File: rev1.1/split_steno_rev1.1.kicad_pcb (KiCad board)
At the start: 2 copper layers, 99.4 x 84.8 mm, 77 parts, among them J1 i2c, J2 serial, J3 rgb, J4 icsp, J5 raw, J6 extra, Q1 BC547, SW1 reset, U1 ProMicro

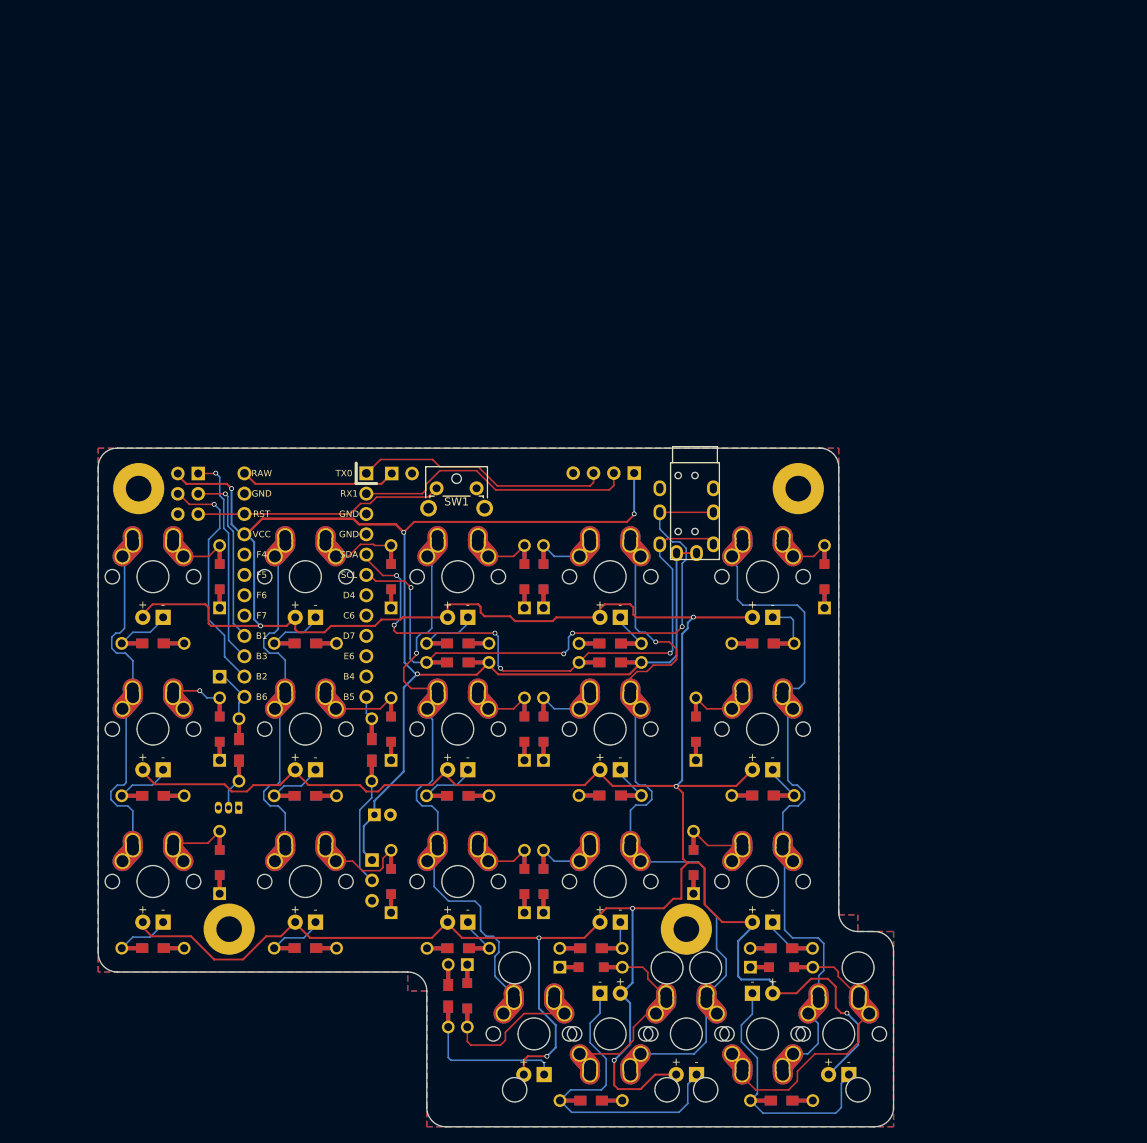
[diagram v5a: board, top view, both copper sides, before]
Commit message: removed led from rev1.1, moved to rev1.2
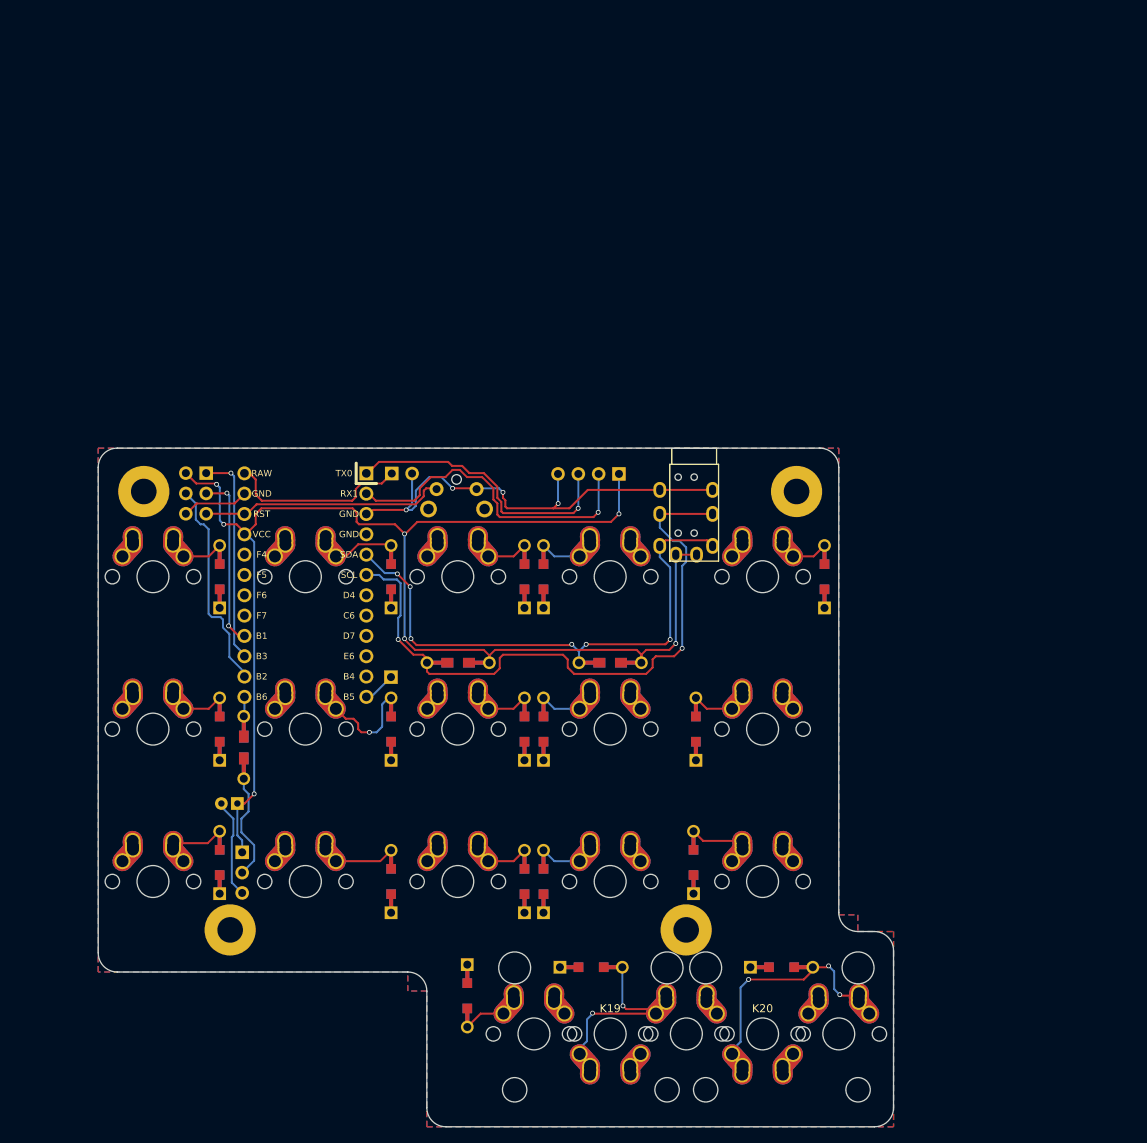
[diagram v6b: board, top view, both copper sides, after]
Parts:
- removed the G*** at (96.1, 158.9) (x2)
- removed MX1, MX10, MX11, MX12, MX13, MX14, MX15, MX16, MX18, MX2, MX20, MX3, MX4, MX5, MX6, MX7, MX8, MX9: MX-1U, Keebio-Parts:Hybrid_PCB_100H_Dual_hole-LED
- removed MX17, MX19: MX-1U, Keebio-Parts:Hybrid_PCB_200H-dual-LED
- removed Q1: BC547, TO_SOT_Packages_THT:TO-92_Inline_Narrow_Oval
- removed R10, R11, R12, R13, R14, R15, R16, R17, R18, R4, R5, R6, R7, R8, R9: 51, Keebio-Parts:Resistor-Hybrid
- removed R19: 470, Keebio-Parts:Resistor-Hybrid
- removed R20: 1k, Keebio-Parts:Resistor-Hybrid
- removed R21, R22: 4.7k, Keebio-Parts:Resistor-Hybrid
- removed the REF** at (55.4, 84.2)
- removed the REF** at (137.8, 84.2)
- removed the REF** at (123.8, 139.3)
- removed the REF** at (66.7, 139.3)
- added G***: LOGO, airi_logo:airi_icon-7.6, B.Cu at (96.2, 159.2)
- added G***: LOGO, airi_logo:airi_icon-7.6, F.Cu at (96.2, 159.2)
- added K1: KEYSW, Keebio-Parts:Hybrid_PCB_100H_Dual_hole, F.Cu at (57.1, 95.2)
- added K10: KEYSW, Keebio-Parts:Hybrid_PCB_100H_Dual_hole-flip, F.Cu at (133.3, 114.3)
- added K11: KEYSW, Keebio-Parts:Hybrid_PCB_100H_Dual_hole, F.Cu at (57.1, 133.3)
- added K12: KEYSW, Keebio-Parts:Hybrid_PCB_100H_Dual_hole, F.Cu at (76.2, 133.3)
- added K13: KEYSW, Keebio-Parts:Hybrid_PCB_100H_Dual_hole, F.Cu at (95.2, 133.3)
- added K14: KEYSW, Keebio-Parts:Hybrid_PCB_100H_Dual_hole-flip, F.Cu at (114.3, 133.3)
- added K15: KEYSW, Keebio-Parts:Hybrid_PCB_100H_Dual_hole-flip, F.Cu at (133.3, 133.3)
- added K16: KEYSW, Keebio-Parts:Hybrid_PCB_100H_Dual_hole-flip, F.Cu at (104.8, 152.4)
- added K17: KEYSW, Keebio-Parts:Hybrid_PCB_100H_Dual_hole-flip, F.Cu at (123.8, 152.4)
- added K18: KEYSW, Keebio-Parts:Hybrid_PCB_100H_Dual_hole, F.Cu at (142.9, 152.4)
- added K19: KEYSW, Keebio-Parts:Hybrid_PCB_200H-dual-nosilk, F.Cu at (114.3, 152.4)
- added K2: KEYSW, Keebio-Parts:Hybrid_PCB_100H_Dual_hole, F.Cu at (76.2, 95.2)
- added K20: KEYSW, Keebio-Parts:Hybrid_PCB_200H-dual-nosilk, F.Cu at (133.3, 152.4)
- added K3: KEYSW, Keebio-Parts:Hybrid_PCB_100H_Dual_hole, F.Cu at (95.2, 95.2)
- added K4: KEYSW, Keebio-Parts:Hybrid_PCB_100H_Dual_hole-flip, F.Cu at (114.3, 95.2)
- added K5: KEYSW, Keebio-Parts:Hybrid_PCB_100H_Dual_hole, F.Cu at (133.3, 95.2)
- added K6: KEYSW, Keebio-Parts:Hybrid_PCB_100H_Dual_hole, F.Cu at (57.1, 114.3)
- added K7: KEYSW, Keebio-Parts:Hybrid_PCB_100H_Dual_hole, F.Cu at (76.2, 114.3)
- added K8: KEYSW, Keebio-Parts:Hybrid_PCB_100H_Dual_hole, F.Cu at (95.2, 114.3)
- added K9: KEYSW, Keebio-Parts:Hybrid_PCB_100H_Dual_hole-flip, F.Cu at (114.3, 114.3)
- added REF**: , Mounting_Holes:MountingHole_3.2mm_M3_Pad, F.Cu at (56.0, 84.6)
- added REF**: , Mounting_Holes:MountingHole_3.2mm_M3_Pad, F.Cu at (137.6, 84.6)
- added REF**: , Mounting_Holes:MountingHole_3.2mm_M3_Pad, F.Cu at (66.8, 139.4)
- added REF**: , Mounting_Holes:MountingHole_3.2mm_M3_Pad, F.Cu at (123.8, 139.4)
- R1, R2: value 51 -> 4.7k
- R3: value 51 -> 470
- REF**: value i2c -> TRRS-PJ-320A
- SW1: moved to B.Cu
- moved R1 57.2 mm to (114.3, 106.0)
- moved R3 29.7 mm to (68.5, 116.6), turned to 270 degrees
- moved J6 21.4 mm to (86.9, 107.8)
- moved R2 19.3 mm to (95.3, 106.0)
- moved C1 17.2 mm to (67.7, 123.6), turned to 180 degrees
- moved J3 16.3 mm to (68.3, 129.7)
- moved SW1 5.00 mm to (97.6, 84.3), turned to 180 degrees
- moved J2 1.90 mm to (115.4, 82.4)
- moved J4 1.00 mm to (63.8, 82.3)
- moved REF** 0.22 mm to (124.8, 81.2)
- moved J1 0.20 mm to (122.8, 81.2)
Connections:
- J6 pad 1: /d4 -> /d3
- R1 pad 1: Net-(MX1-Pad4) -> /d1
- R1 pad 2: Net-(Q1-Pad1) -> VCC
- R2 pad 1: Net-(MX2-Pad4) -> /d2
- R2 pad 2: Net-(Q1-Pad1) -> VCC
- R3 pad 1: Net-(MX3-Pad4) -> Net-(J3-Pad2)
- R3 pad 2: Net-(Q1-Pad1) -> /d4
- SW1 pad 1: /rst -> GND
- SW1 pad 2: GND -> /rst
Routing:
- net VCC: track 595.1 -> 181.4 mm, vias 12 -> 7
- net /c4: track 87.6 -> 0.00 mm, vias 1 -> 0
- net GND: track 0.00 -> 79.9 mm, vias 0 -> 4
- net /c5: track 78.5 -> 0.00 mm
- net /c3: track 68.7 -> 0.00 mm, vias 1 -> 0
- net /c1: track 43.0 -> 0.00 mm
- net /c2: track 41.4 -> 0.00 mm
- net Net-(MX17-Pad4): track 40.5 -> 0.00 mm
- net Net-(MX19-Pad4): track 32.0 -> 0.00 mm
- net Net-(MX16-Pad4): track 17.5 -> 0.00 mm
- net Net-(D16-Pad2): track 18.8 -> 6.42 mm
- net /d1: track 78.2 -> 68.3 mm, vias 5 -> 6
- net Net-(MX3-Pad4): track 6.96 -> 0.00 mm
- net Net-(MX6-Pad4): track 6.87 -> 0.00 mm
- net Net-(MX8-Pad4): track 6.81 -> 0.00 mm
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
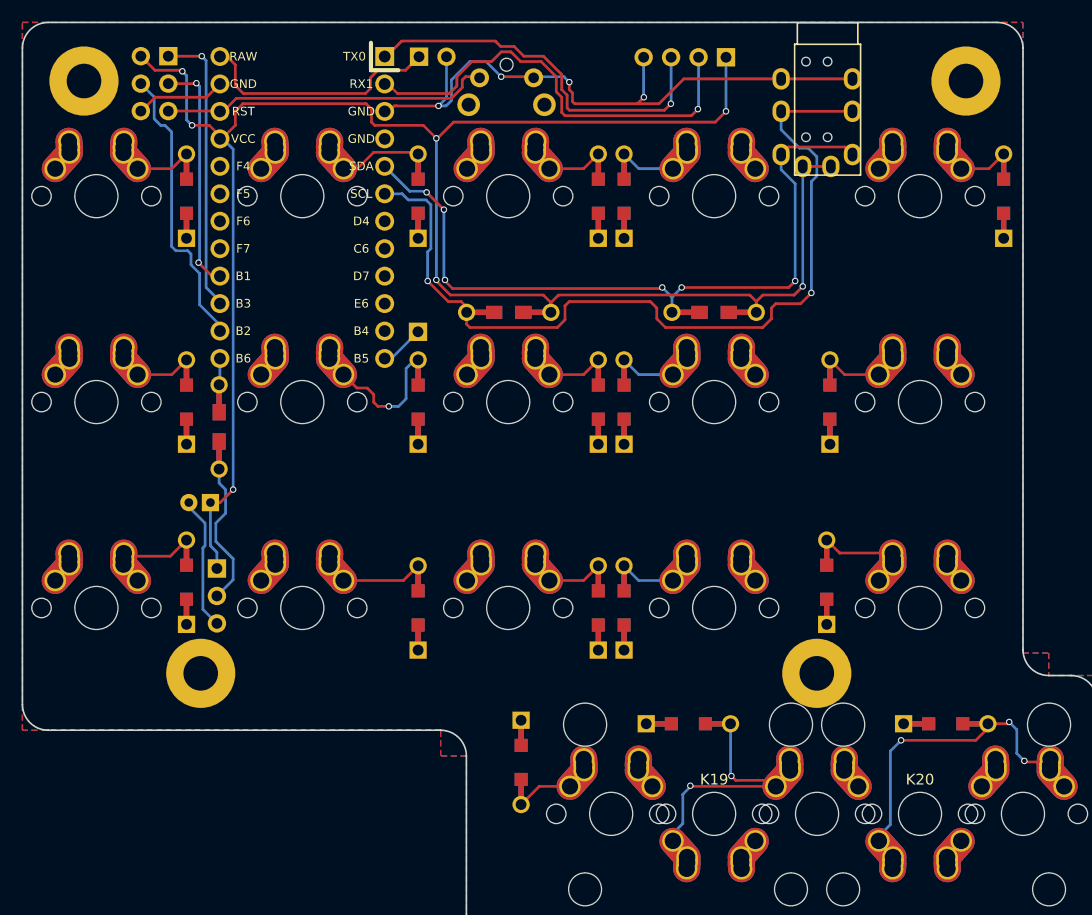
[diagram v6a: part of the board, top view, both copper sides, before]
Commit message: finished routing, added silkscreen
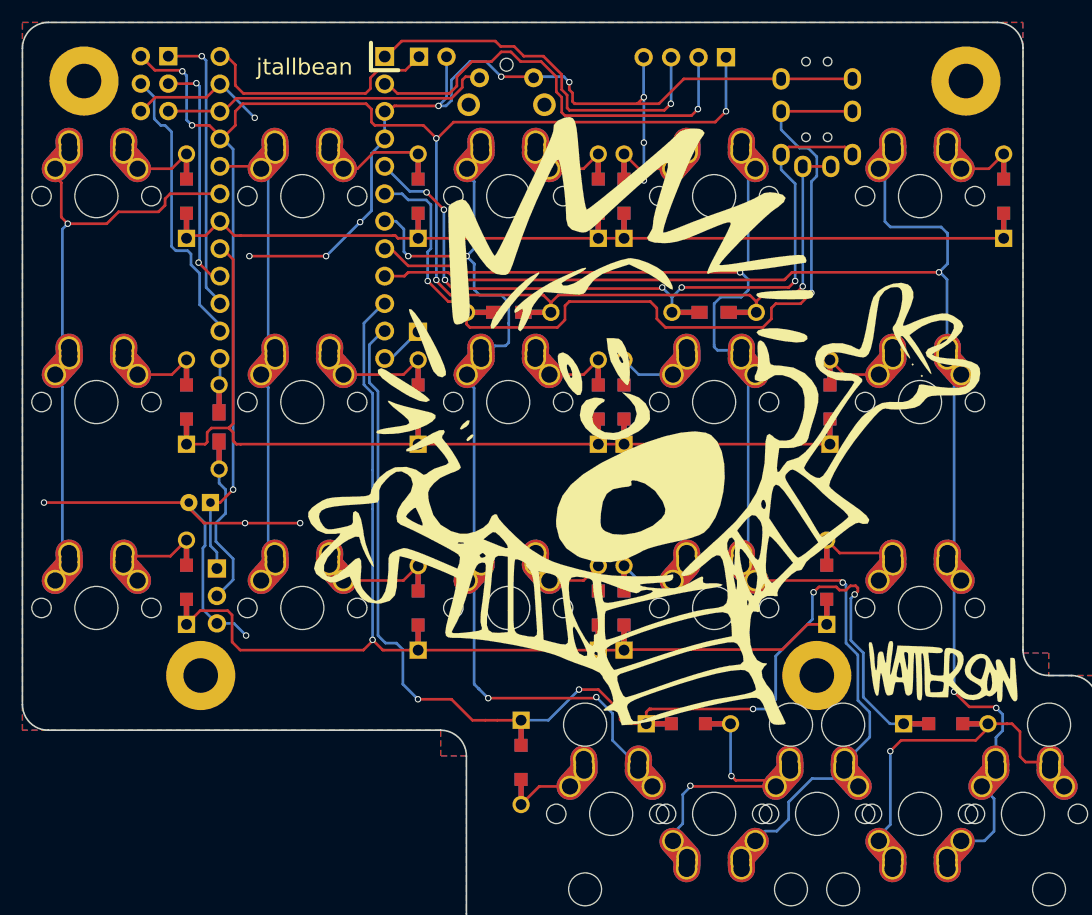
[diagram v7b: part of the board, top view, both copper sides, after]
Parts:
- added G***: LOGO, lib_fp:hobbes, B.Cu at (110.2, 117.9)
- added G***: LOGO, lib_fp:calvin, F.Cu at (107.8, 115.8)
- added G***: LOGO, lib_fp:watterson, F.Cu at (135.4, 139.2)
- added G***: LOGO, lib_fp:watterson, B.Cu at (58.1, 122.5)
- moved REF** 0.20 mm to (66.8, 139.6)
- moved REF** 0.20 mm to (123.8, 139.6)
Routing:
- net /c5: track 0.00 -> 124.1 mm, vias 0 -> 3
- net /c4: track 0.00 -> 117.7 mm, vias 0 -> 2
- net /r4: track 0.00 -> 111.1 mm, vias 0 -> 5
- net /r3: track 0.00 -> 102.8 mm, vias 0 -> 1
- net /r1: track 0.00 -> 85.4 mm
- net /r2: track 0.00 -> 85.2 mm
- net /c3: track 0.00 -> 84.0 mm, vias 0 -> 4
- net GND: track 79.9 -> 142.9 mm, vias 4 -> 14
- net /c1: track 0.00 -> 56.2 mm, vias 0 -> 1
- net /c2: track 0.00 -> 43.2 mm
- net Net-(D7-Pad2): track 13.2 -> 10.2 mm, vias 1 -> 0
- net Net-(D4-Pad2): track 5.09 -> 6.29 mm
- net Net-(D18-Pad2): vias 3 -> 1
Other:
- board text added: "jtallbean"
- board text added: "rev1.1"
